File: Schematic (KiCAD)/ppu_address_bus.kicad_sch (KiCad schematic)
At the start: 56 parts, among them X3 INVERT

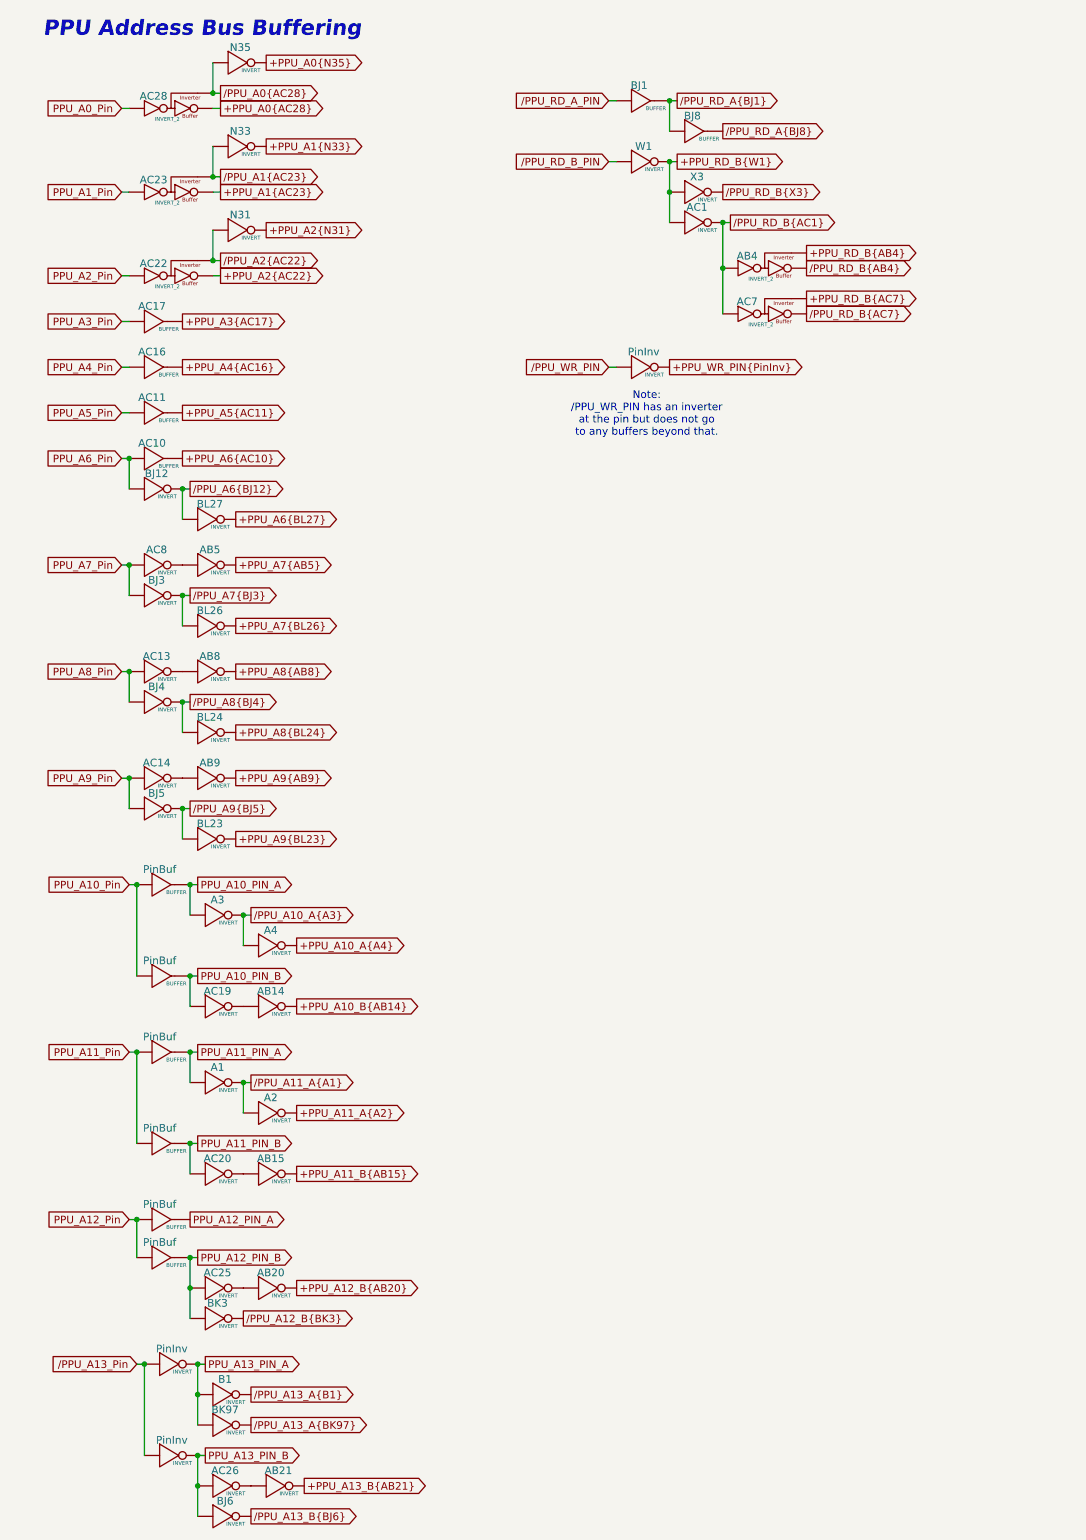
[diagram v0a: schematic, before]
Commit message: - Started work on the pulse channels.  - Solved at least 2 of the red traces in the SVG.  - Finally realized that "Unknown 4to1" cells are actually just ordinary And-Or-Invert "AOI22" cells.
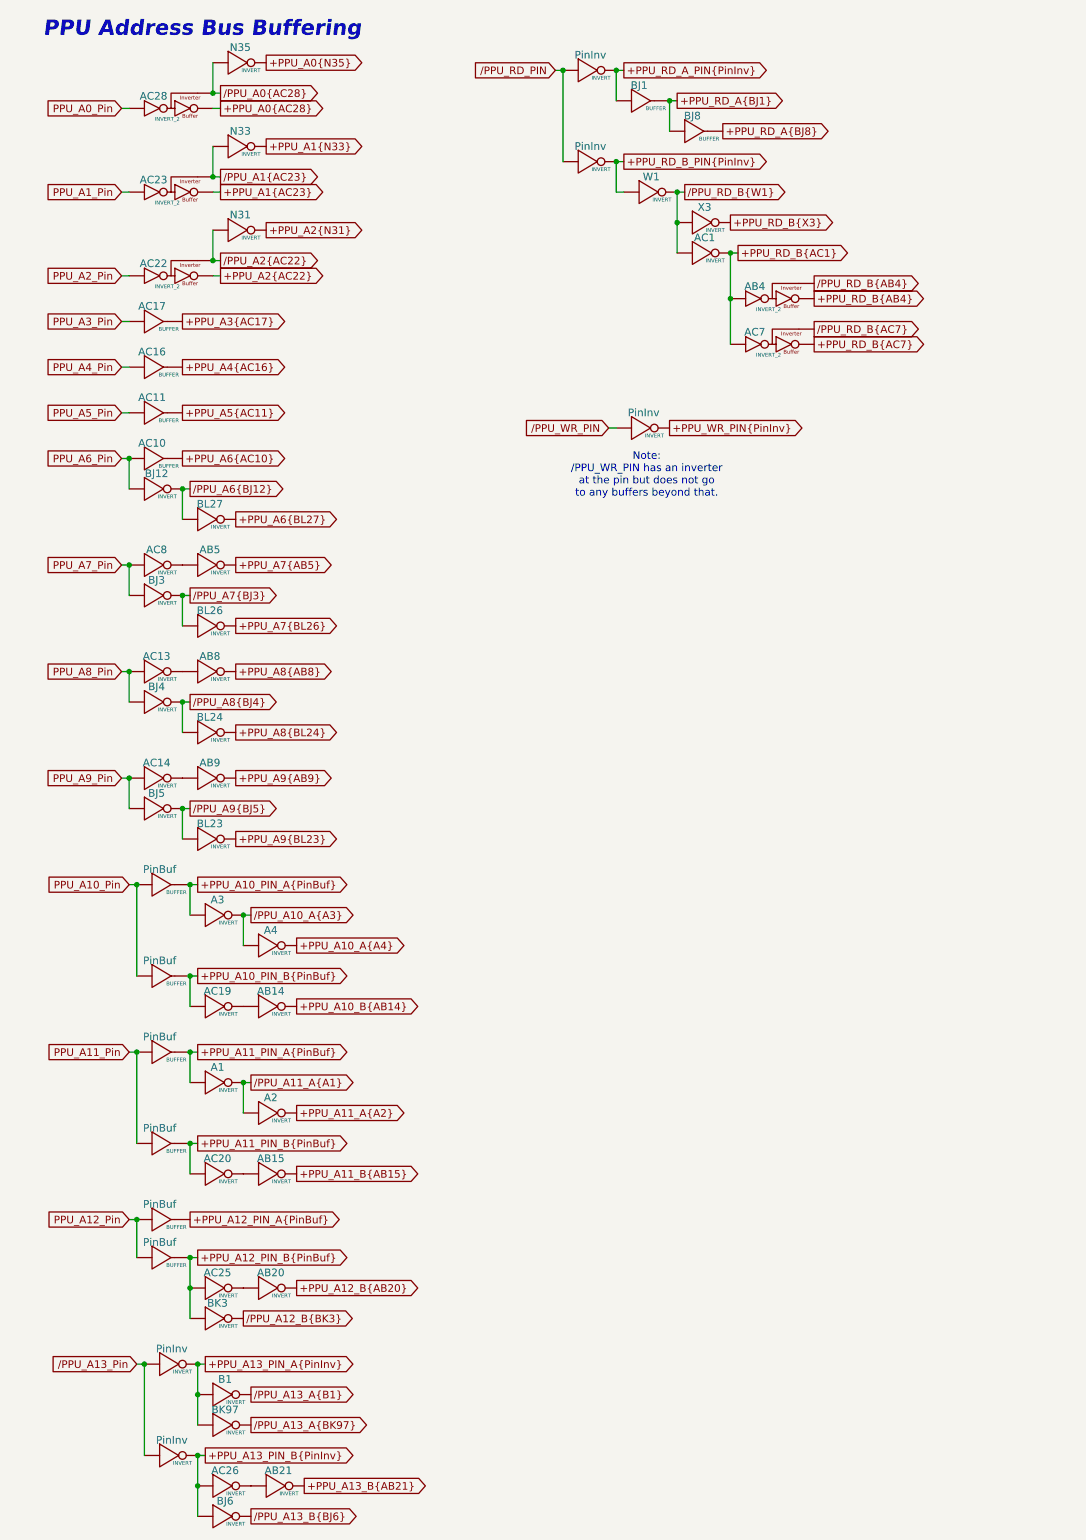
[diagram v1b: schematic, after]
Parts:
- added PinInv (x2): INVERT, symbol MMC5:INVERT
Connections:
- net PPU_A12_PIN_A is gone; now on net PPU_A12_Pin: PinBuf. (X)
- net /PPU_RD_A{BJ8} is gone; now on net +PPU_RD_A{BJ8}: BJ8. (X)
- net /PPU_RD_B_PIN is gone; now on net /PPU_RD_B{W1}: W1. (X)
- net /PPU_RD_B{X3} is gone; now on net /PPU_RD_B{W1}: X3. (X)
- net +PPU_A13_PIN_B{PinInv}: now reaches AC26. (X)
- net +PPU_A13_PIN_B{PinInv}: now also BJ6. (X), PinInv. (X); no longer AB21. (X)
- net +PPU_A11_PIN_B{PinBuf}: now reaches AC20. (X)
- net +PPU_A11_PIN_B{PinBuf}: now also PinBuf. (X); no longer AB15. (X)
- net +PPU_A12_PIN_B{PinBuf}: now reaches AC25. (X)
- net +PPU_A12_PIN_B{PinBuf}: now also BK3. (X), PinBuf. (X); no longer AB20. (X)
- net +PPU_A10_PIN_B{PinBuf}: now reaches AC19. (X)
- net +PPU_A10_PIN_B{PinBuf}: now also PinBuf. (X); no longer AB14. (X)
- net +PPU_RD_B{W1} renamed /PPU_RD_B{W1}
- removed net PPU_A10_PIN_A: A3. (X), PinBuf. (X)
- removed net PPU_A10_PIN_B: AC19. (X), PinBuf. (X)
- removed net PPU_A11_PIN_A: A1. (X), PinBuf. (X)
- removed net PPU_A11_PIN_B: AC20. (X), PinBuf. (X)
- removed net PPU_A12_PIN_B: AC25. (X), BK3. (X), PinBuf. (X)
- removed net PPU_A13_PIN_A: B1. (X), BK97. (X), PinInv. (X)
- removed net PPU_A13_PIN_B: AC26. (X), BJ6. (X), PinInv. (X)
- net /PPU_RD_A_PIN renamed +PPU_RD_A{BJ1}
- net +PPU_RD_A{BJ1}: now also BJ8. (X)
- net /PPU_RD_A{BJ1} renamed +PPU_RD_A{BJ8}
- net +PPU_RD_A{BJ8}: no longer BJ1. (X)
- removed net /PPU_RD_B{AC1}: AB4. (X), AC1. (X), AC7. (X)
- new net: AB21. (X), AC26. (X)
- new net: AB15. (X), AC20. (X)
- new net: AB5. (X), AC8. (X)
- new net: AB9. (X), AC14. (X)
- new net: AB20. (X), AC25. (X)
- new net: AB14. (X), AC19. (X)
- new net: AB8. (X), AC13. (X)
- new net +PPU_A10_PIN_A{PinBuf}: A3. (X), PinBuf. (X)
- new net +PPU_A11_PIN_A{PinBuf}: A1. (X), PinBuf. (X)
- new net +PPU_A12_PIN_A{PinBuf}: PinBuf. (X)
- new net +PPU_A13_PIN_A{PinInv}: B1. (X), BK97. (X), PinInv. (X)
- new net +PPU_RD_A_PIN{PinInv}: BJ1. (X), PinInv. (X)
- new net +PPU_RD_B_PIN{PinInv}: PinInv. (X), W1. (X)
- new net +PPU_RD_B{AC1}: AB4. (X), AC1. (X), AC7. (X)
- new net +PPU_RD_B{X3}: X3. (X)
- new net /PPU_RD_PIN: PinInv. (X), PinInv. (X)
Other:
- moved on the sheet: AB4, AC1, AC7, PinInv, W1, X3

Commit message: - Pulse DAC logic is now complete.  - The 4-bit adders are verified correct using Excel.    - This revealed 1 tracing error and also 3 XNOR gates that are actually XOR in this case.  - Now including a PDF version of the schematic.
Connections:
- new net: AB21. (X), AC26. (X)
- new net: AB15. (X), AC20. (X)
- new net: AB5. (X), AC8. (X)
- new net: AB9. (X), AC14. (X)
- new net: AB20. (X), AC25. (X)
- new net: AB14. (X), AC19. (X)
- new net: AB8. (X), AC13. (X)

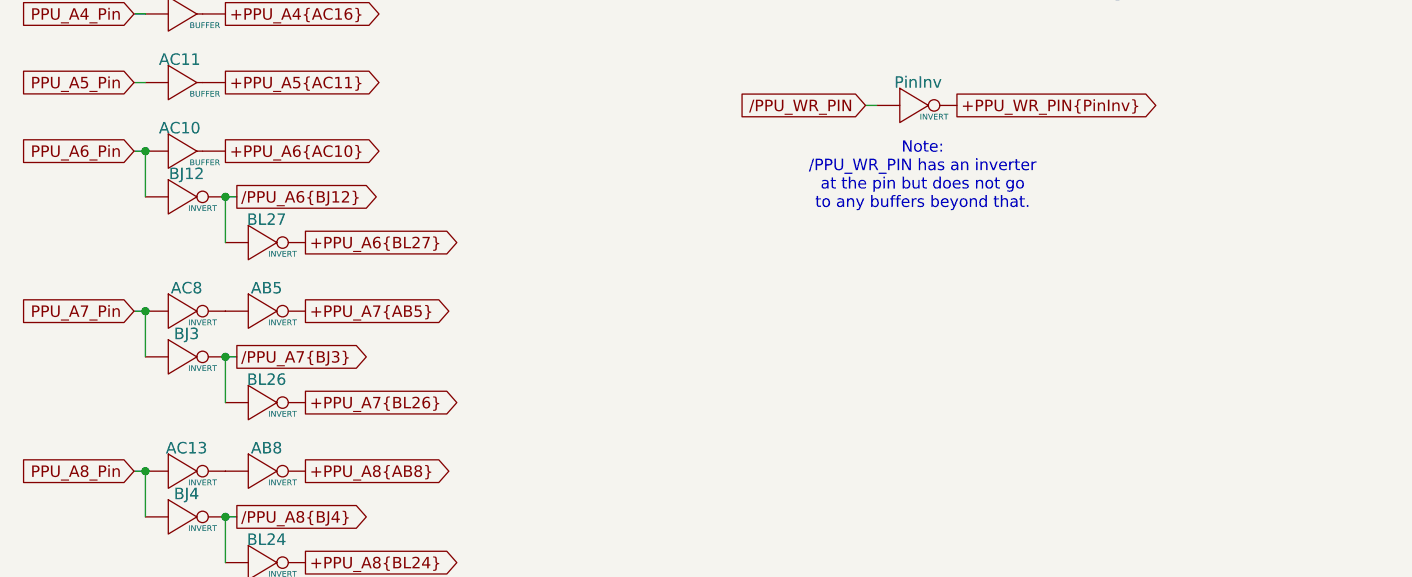
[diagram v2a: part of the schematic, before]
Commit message: Schematic Updates:  - Added all 10-bit CHR banking registers $5120 - $512B, including where all 10 bits come from when written.  - Added 8-bit CHR bank register $5202, which is the bank used when rendering the V-Split region.    + V-Split seems to always be 8-bit, 8kB bank regardless of CHR mode.  The wiki doesn't say that and I don't know for sure.  - Added decoding logic that activates the correct CHR bank for CHR A10, A11, A12 (corresponding to columns AV, AW, AX).  - Noted, AX15 activates $5202 CHR Bank for V-Split region.  AX16 activates CHR Bank from data stored in ExRAM for extended attributes.  Therefore, AX15 driven by AT1 High means we specifically are in v-split region, and not extended attribute mode.  With this knowledge, backtracking up the chain from AT1 to N14 sheds very useful insight what the 3-bit shift register at N11/N12/N13 is doing.  We now know that N14 goes low specifically for pattern table fetches when rendering the V-split region, and does not appear dual-purposed for extended attribute fetch sequencing.  This may seem rather subtle or unimportant, but it is a good advancement for higher level understanding what that mysterious shift register might be doing.
SVG Trace Updates:
 - Registers $5120, 5121, 5122, 5123 (first 4 CHR bank register), the outputs were labeled in reverse order.
 - Register $5130 (highest CHR bank bits), the outputs were labeled with backwards polarity.  The error was not having taken into account that the CPU data bus input to the latches came already inverted to begin with.
 - Still wrong: Cell AV7, 2-input NAND gate.  One of the inputs is missing and it logically should be driven by AS19 like the 4 cells to its direct right.  I can't quite make out how it makes that connection.
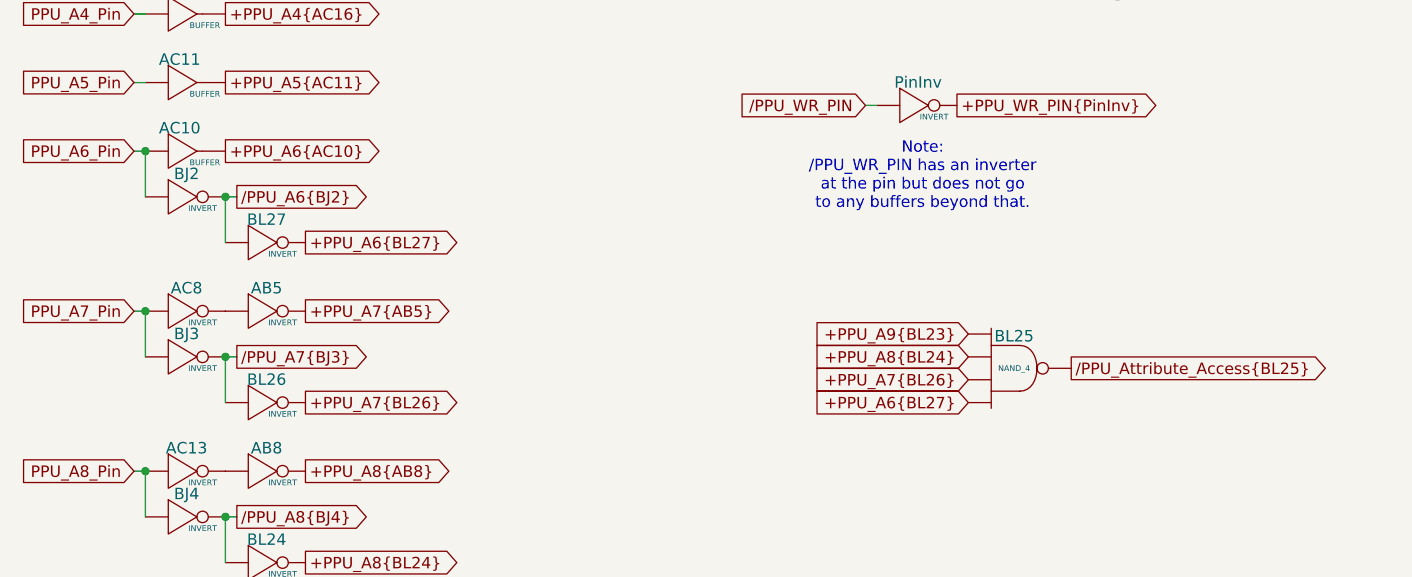
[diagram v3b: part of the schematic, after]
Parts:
- added BL25: NAND_4, symbol MMC5:NAND_4
- renumbered BJ12 to BJ2
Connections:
- net +PPU_A6{BL27}: now also BL25. (X)
- net +PPU_A7{BL26}: now also BL25. (X)
- net +PPU_A8{BL24}: now also BL25. (X)
- net +PPU_A9{BL23}: now also BL25. (X)
- net /PPU_A6{BJ12} renamed /PPU_A6{BJ2}
- new net: AB21. (X), AC26. (X)
- new net: AB15. (X), AC20. (X)
- new net: AB5. (X), AC8. (X)
- new net: AB9. (X), AC14. (X)
- new net: AB20. (X), AC25. (X)
- new net: AB14. (X), AC19. (X)
- new net: AB8. (X), AC13. (X)
- new net /PPU_Attribute_Access{BL25}: BL25. (X)
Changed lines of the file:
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@@
 		)
 	)
+	(global_label "{slash}PPU_Attribute_Access{BL25}"
+		(shape output)
+		(at 133.35 111.76 0)
+		(fields_autoplaced yes)
+		(effects
+			(font
+				(size 1.27 1.27)
+			)
+			(justify left)
+		)
+		(property "Intersheetrefs" "${INTERSHEET_REFS}"
+			(at 164.3358 111.76 0)
+			(effects
+				(font
+					(size 1.27 1.27)
+				)
+				(justify left)
+				(hide yes)
+			)
+		)
+	)
 	(global_label "{slash}PPU_RD_PIN"
 		(shape input)
@@
 		)
 	)
+	(global_label "+PPU_A7{BL26}"
+		(shape input)
+		(at 121.92 113.03 180)
+		(fields_autoplaced yes)
+		(effects
+			(font
+				(size 1.27 1.27)
+			)
+			(justify right)
+		)
+		(property "Intersheetrefs" "${INTERSHEET_REFS}"
+			(at 103.8157 113.03 0)
+			(effects
+				(font
+					(size 1.27 1.27)
+				)
+				(justify right)
+				(hide yes)
+			)
+		)
+	)
 	(global_label "PPU_A6_Pin"
 		(shape input)
@@
 		)
 	)
+	(global_label "+PPU_A9{BL23}"
+		(shape input)
+		(at 121.92 107.95 180)
+		(fields_autoplaced yes)
+		(effects
+			(font
+				(size 1.27 1.27)
+			)
+			(justify right)
+		)
+		(property "Intersheetrefs" "${INTERSHEET_REFS}"
+			(at 103.8157 107.95 0)
+			(effects
+				(font
+					(size 1.27 1.27)
+				)
+				(justify right)
+				(hide yes)
+			)
+		)
+	)
 	(global_label "+PPU_A13_PIN_B{PinInv}"
 		(shape output)
@@
 		)
 	)
+	(global_label "+PPU_A6{BL27}"
+		(shape input)
+		(at 121.92 115.57 180)
+		(fields_autoplaced yes)
+		(effects
+			(font
+				(size 1.27 1.27)
+			)
+			(justify right)
+		)
+		(property "Intersheetrefs" "${INTERSHEET_REFS}"
+			(at 103.8157 115.57 0)
+			(effects
+				(font
+					(size 1.27 1.27)
+				)
+				(justify right)
+				(hide yes)
+			)
+		)
+	)
 	(global_label "+PPU_RD_A{BJ1}"
 		(shape output)
@@
 		)
 	)
+	(global_label "+PPU_A8{BL24}"
+		(shape input)
+		(at 121.92 110.49 180)
+		(fields_autoplaced yes)
+		(effects
+			(font
+				(size 1.27 1.27)
+			)
+			(justify right)
+		)
+		(property "Intersheetrefs" "${INTERSHEET_REFS}"
+			(at 103.8157 110.49 0)
+			(effects
+				(font
+					(size 1.27 1.27)
+				)
+				(justify right)
+				(hide yes)
+			)
+		)
+	)
 	(global_label "+PPU_A0{N35}"
 		(shape output)
@@
 		)
 	)
-	(global_label "{slash}PPU_A6{BJ12}"
+	(global_label "{slash}PPU_A6{BJ2}"
 		(shape output)
 		(at 40.64 92.71 0)
@@
 		)
 		(property "Intersheetrefs" "${INTERSHEET_REFS}"
-			(at 58.4419 92.71 0)
+			(at 57.2324 92.71 0)
 			(effects
 				(font
@@
 	)
 	(symbol
+		(lib_name "NAND_4_1")
+		(lib_id "MMC5:NAND_4")
+		(at 127 111.76 0)
+		(unit 1)
+		(exclude_from_sim no)
+		(in_bom yes)
+		(on_board yes)
+		(dnp no)
+		(fields_autoplaced yes)
+		(property "Reference" "BL25"
+			(at 127 107.442 0)
+			(do_not_autoplace yes)
+			(effects
+				(font
+					(size 1.27 1.27)
+				)
+				(justify top)
+			)
+		)
+		(property "Value" "NAND_4"
+			(at 127 111.76 0)
+			(do_not_autoplace yes)
+			(effects
+				(font
+					(size 0.635 0.635)
+				)
+			)
+		)
+		(property "Footprint" ""
+			(at 127 111.76 0)
+			(effects
+				(font
+					(size 1.27 1.27)
+				)
+				(hide yes)
+			)
+		)
+		(property "Datasheet" ""
+			(at 127 111.76 0)
+			(effects
+				(font
+					(size 1.27 1.27)
+				)
+				(hide yes)
+			)
+		)
+		(property "Description" ""
+			(at 127 111.76 0)
+			(effects
+				(font
+					(size 1.27 1.27)
+				)
+				(hide yes)
+			)
+		)
+		(pin ""
+		)
+		(pin ""
+		)
+		(pin ""
+		)
+		(pin ""
+		)
+		(pin ""
+		)
+		(instances
+			(project "MMC5"
+				(path "/46093bf6-f83e-4237-9ece-7350a682aff0/ea105755-ff0d-4162-b72d-5fd0cda1402e"
+					(reference "BL25")
+					(unit 1)
+				)
+			)
+		)
+	)
+	(symbol
 		(lib_name "INVERT_25")
 		(lib_id "MMC5:INVERT")
@@
 		(dnp no)
 		(fields_autoplaced yes)
-		(property "Reference" "BJ12"
+		(property "Reference" "BJ2"
 			(at 35.052 89.408 0)
 			(do_not_autoplace yes)
@@
 			(project ""
 				(path "/46093bf6-f83e-4237-9ece-7350a682aff0/ea105755-ff0d-4162-b72d-5fd0cda1402e"
-					(reference "BJ12")
+					(reference "BJ2")
 					(unit 1)
 				)
